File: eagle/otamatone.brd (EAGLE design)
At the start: 65 x 43.3 mm, 55 parts, among them IC1 TDA2822MSOP8, K1 MK20DX256VLH7

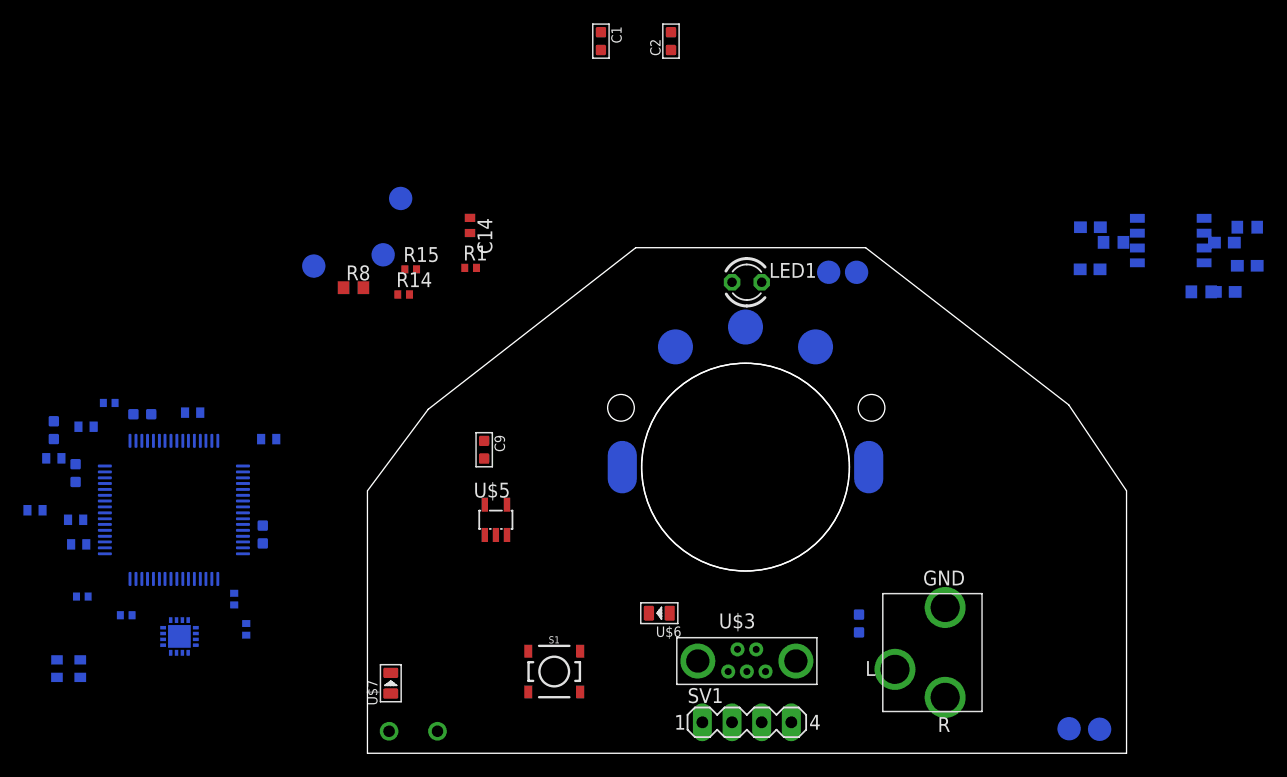
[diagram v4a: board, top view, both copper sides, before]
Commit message: started laying out pcb
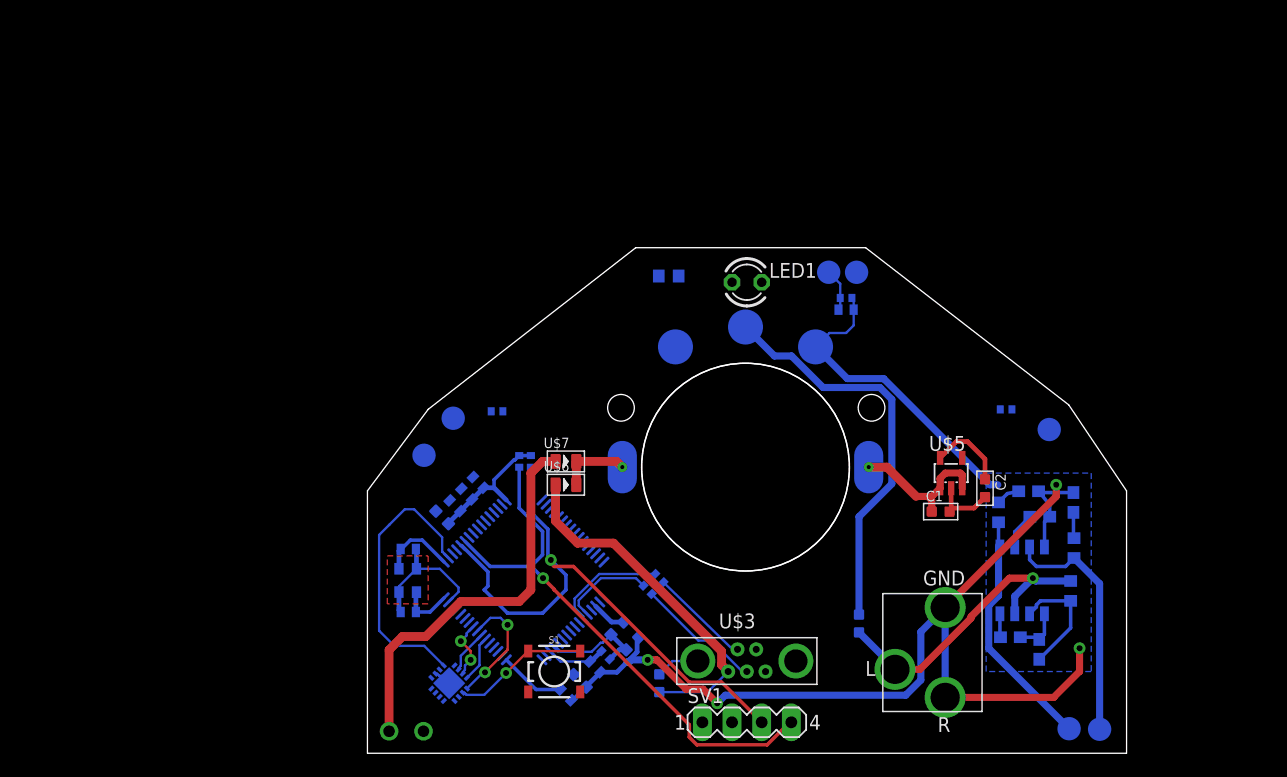
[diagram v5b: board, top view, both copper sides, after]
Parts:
- moved SX2 64.5 mm to (58.4, 27.7)
- moved C6 52.8 mm to (22.7, 9.40), turned to 225 degrees
- moved R15 52.4 mm to (54.7, 29.5), flipped to the bottom
- moved C1 49.7 mm to (49.1, 20.7), turned to 90 degrees
- moved R5 49.4 mm to (25.0, 15.0), turned to 45 degrees
- moved C8 48.3 mm to (17.0, 5.00), turned to 225 degrees
- moved C7 48.2 mm to (19.5, 7.40), turned to 225 degrees
- moved R3 47.7 mm to (20.4, 8.40), turned to 45 degrees
- moved C2 46.8 mm to (52.9, 22.7), turned to 0 degrees
- moved R6 44.7 mm to (24.0, 14.0), turned to 45 degrees
- moved R2 44.6 mm to (21.4, 10.7), turned to 135 degrees
- moved U$5 39.2 mm to (50.0, 24.0)
- moved C15 35.8 mm to (55.1, 9.94), turned to 180 degrees
- moved C19 34.6 mm to (9.50, 23.2), turned to 45 degrees
- moved C10 33.1 mm to (3.50, 12.1)
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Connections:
- net N$10 renamed USB0_DP
- net N$14 renamed USB0_DM
- net N$16 renamed USB_P
- net N$17 renamed USB_M
- net N$1: now also U$1.0; no longer U$1.1
- net VIN: now also U$1.1; no longer U$1.0
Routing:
- net AGND: track 0.00 -> 125.5 mm, vias 0 -> 4
- net SCL0: track 0.00 -> 49.3 mm, vias 0 -> 1
- net SDA0: track 0.00 -> 46.4 mm, vias 0 -> 1
- net VOL_OUT: track 0.00 -> 34.7 mm
- net VBAT: track 0.00 -> 33.8 mm
- net VUSB: track 0.00 -> 30.6 mm
- net SOUND: track 0.00 -> 26.6 mm, vias 0 -> 1
- net VCC: track 0.00 -> 24.3 mm
- net N$12: track 0.00 -> 24.3 mm
- net GND: track 0.00 -> 22.6 mm
- net S+: track 0.00 -> 21.1 mm
- net S-: track 0.00 -> 21.0 mm
- net VIN: track 0.00 -> 13.0 mm, vias 0 -> 1
- net N$9: track 0.00 -> 11.7 mm, vias 0 -> 1
- net USB_P: track 0.00 -> 10.9 mm
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- added copper zone on layer 16, net AGND
- added copper zone on layer 1, net N$4

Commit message: first pass at routing board
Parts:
- removed BTN_GND, SX5: PINSMT, otamatone:SMD
- removed C10, C11: 22pF, otamatone:C0402
- added SX1, SX3, SX4: PIN, otamatone:PTH_39MIL
- SX2: value PINSMT -> PIN; device otamatone:SMD -> otamatone:PTH_39MIL
- moved R15 37.5 mm to (17.2, 28.2)
- moved R14 5.41 mm to (16.0, 27.0)
- moved SX2 2.36 mm to (60.0, 26.0), flipped to the top
- moved R9 0.10 mm to (12.9, 25.0)
- turned R8 to 180 degrees
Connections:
- net GND: now also SX1.1, SX3.1; no longer BTN_GND.P$1, C10.2, C11.2, R14.2, R15.2
- net LBUTTON: now also SX2.1; no longer SX5.P$1
- net N$5: no longer C10.1
- net N$6: no longer C11.1
- net RBUTTON: now also SX4.1; no longer SX2.P$1
- net VCC: now also R14.2, R15.2
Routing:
- net VCC: track 24.3 -> 153.1 mm, vias 0 -> 6
- net GND: track 22.6 -> 117.4 mm, vias 0 -> 7
- net FULLVOL: track 0.00 -> 94.1 mm, vias 0 -> 2
- net LBUTTON: track 0.00 -> 86.1 mm, vias 0 -> 2
- net N$19: track 3.77 -> 47.3 mm, vias 0 -> 1
- net 20/NECK: track 3.67 -> 43.7 mm, vias 0 -> 4
- net N$31: track 0.00 -> 32.7 mm, vias 0 -> 2
- net VIN: track 13.0 -> 44.7 mm
- net RBUTTON: track 0.00 -> 29.4 mm, vias 0 -> 2
- net N$12: track 24.3 -> 33.0 mm, vias 0 -> 2
- net N$3: track 10.3 -> 18.2 mm
- net N$52: track 0.00 -> 7.69 mm
- net AGND: track 125.5 -> 131.7 mm
- net SCL0: track 49.3 -> 47.9 mm
- net N$6: track 6.59 -> 5.76 mm
- added copper zone on layer 1, net GND
- added copper zone on layer 16, net GND
- removed copper zone on layer 1, net N$4
